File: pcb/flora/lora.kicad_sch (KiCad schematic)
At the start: 6 parts, among them J7 U.FL-R-SMT-1_10_, U1 Ai-Thinker-Ra-01H

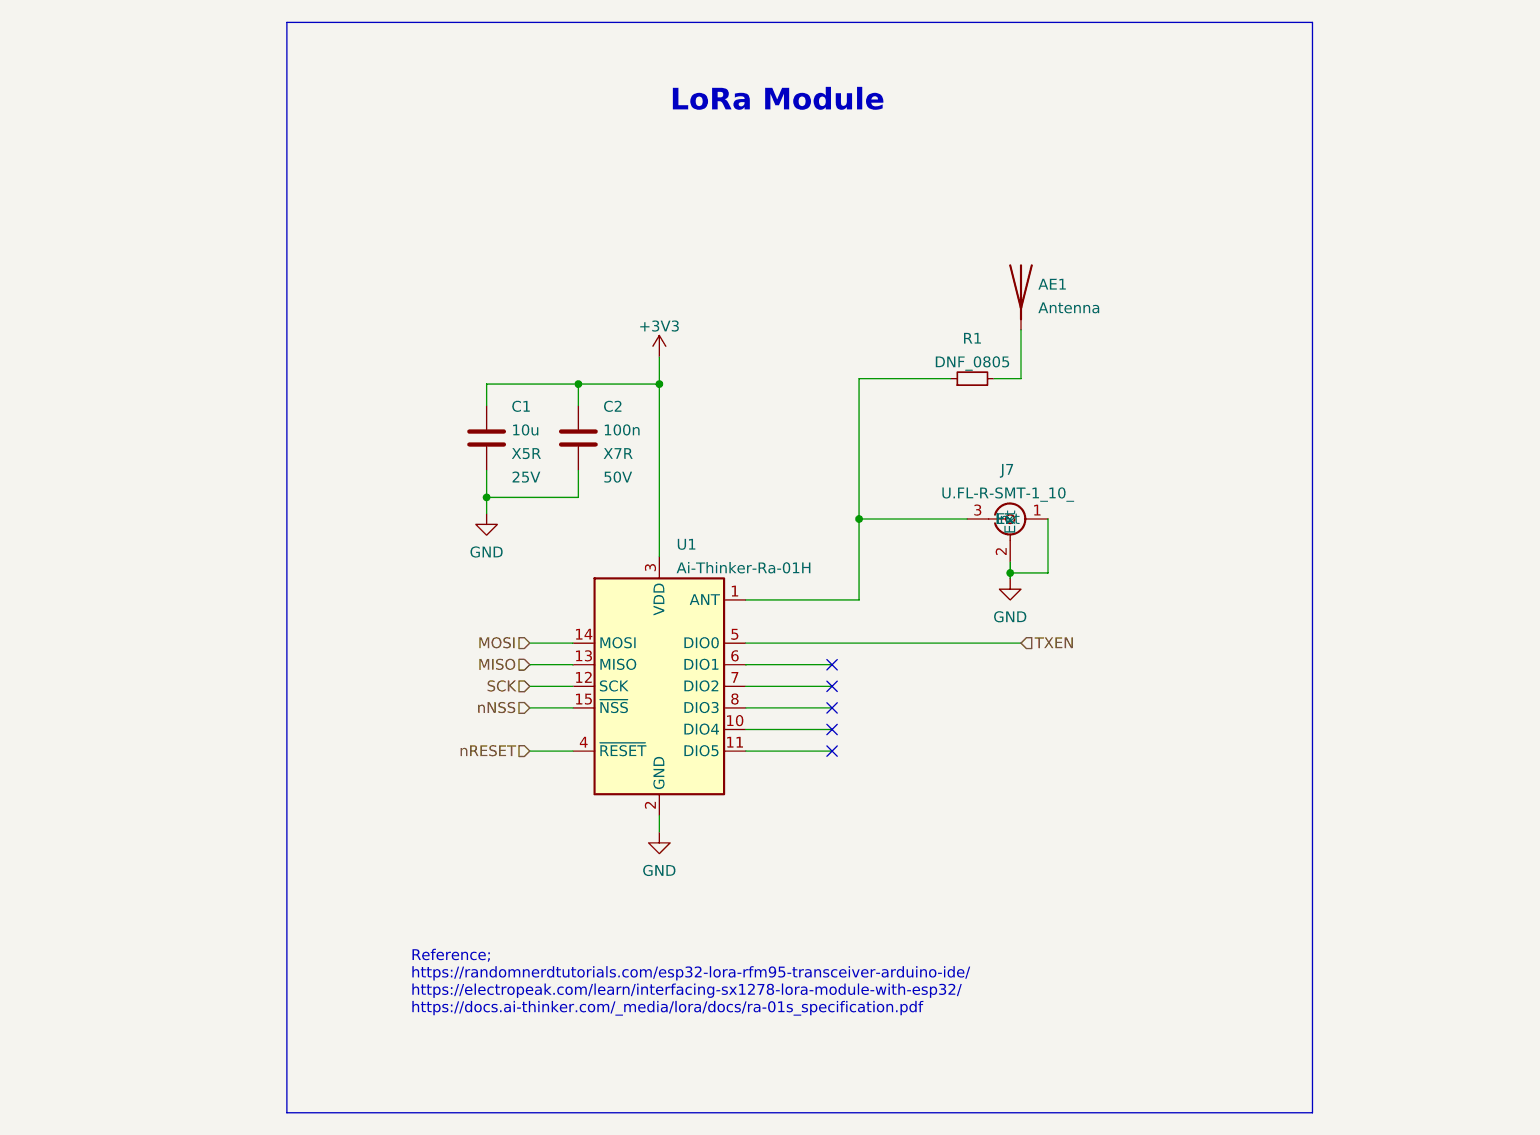
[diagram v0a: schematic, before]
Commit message: replaced ra 01 with rfm95
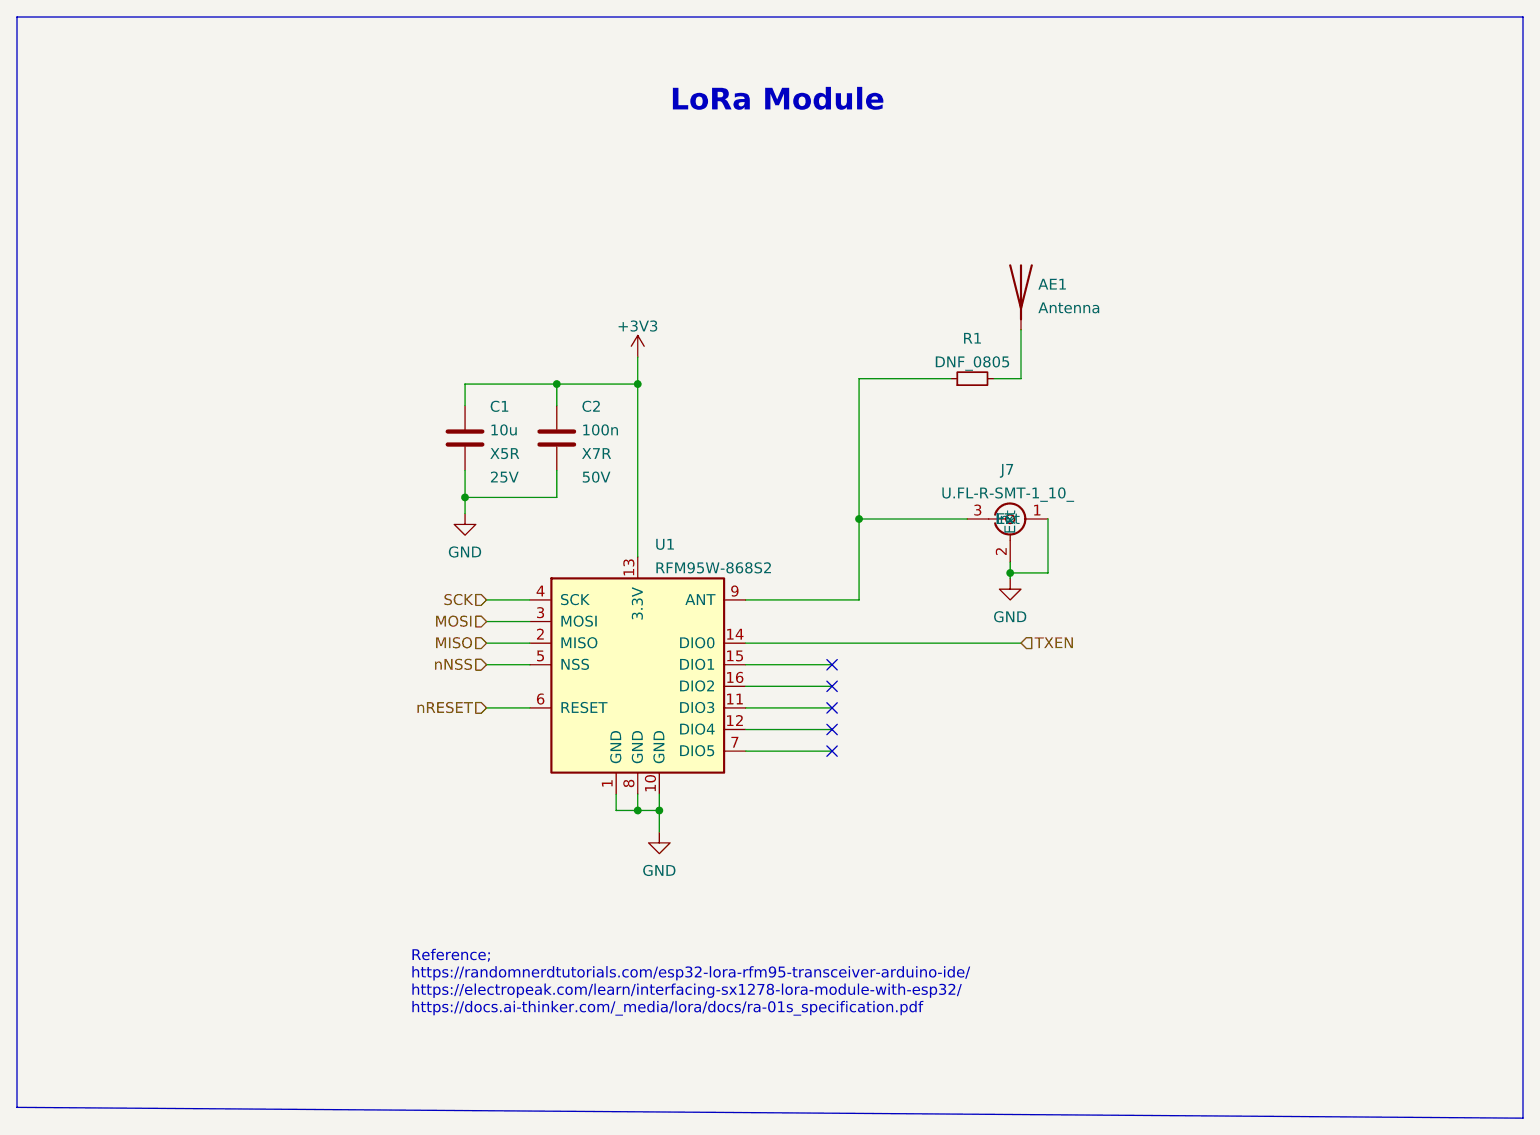
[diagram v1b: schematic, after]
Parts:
- removed U1: Ai-Thinker-Ra-01H, RF_Module:Ai-Thinker-Ra-01-LoRa, symbol RF_JLC:Ai-Thinker-Ra-01H
- added U1: RFM95W-868S2, personal:RFM95W, symbol RF_JLC:RFM95W-868S2
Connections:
- net +3V3: now also U1.13 (3.3V)
- net GND: now also U1.1 (GND), U1.10 (GND), U1.8 (GND)
- net MISO: now also U1.2 (MISO)
- net MOSI: now also U1.3 (MOSI)
- net SCK: now also U1.4 (SCK)
- net TXEN: now also U1.14 (DIO0)
- net nNSS: now also U1.5 (NSS)
- net nRESET: now also U1.6 (RESET)
- net at J7.3 (In), R1.1: now also U1.9 (ANT)
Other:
- moved on the sheet: C1, C2
